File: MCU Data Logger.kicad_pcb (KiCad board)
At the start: 2 copper layers, 29 parts, among them J1 Conn_01x04_Pin, J2 Conn_01x04_Pin, J3 Conn_01x09_Pin, J4 Conn_02x03_Odd_Even, U1 24LC1025, U2 24LC1025, U3 ATmega328P, U4 DS1337S_, Y1 16MHz, Y2 32.768 KHz

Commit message: Components find there home
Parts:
- BT1: footprint TerminalBlock_Phoenix:TerminalBlock_Phoenix_MPT-0,5-2-2.54_1x02_P2.54mm_Horizontal -> Connector_PinHeader_2.54mm:PinHeader_2x01_P2.54mm_Vertical
- moved H1 118.7 mm to (167.5, 66.9)
- moved R7 99.6 mm to (160.5, 43.3)
- moved C4 95.8 mm to (160.5, 45.7)
- moved C3 94.6 mm to (154.3, 63.4)
- moved R3 93.9 mm to (154.3, 41.0)
- moved C2 91.4 mm to (149.7, 63.4)
- moved R2 90.7 mm to (150.7, 41.0), turned to 180 degrees
- moved C1 88.4 mm to (145.1, 63.4)
- moved R1 87.8 mm to (147.3, 41.0)
- moved R4 84.8 mm to (140.5, 63.4), turned to 180 degrees
- moved D1 82.6 mm to (160.5, 41.0)
- moved U3 81.4 mm to (150.9, 50.0)
- moved R5 79.4 mm to (135.9, 63.4), turned to 180 degrees
- moved J1 77.2 mm to (167.0, 52.6)
- moved J2 76.3 mm to (163.2, 67.6), turned to -90 degrees
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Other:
- board outline added: 43.2 x 33 mm

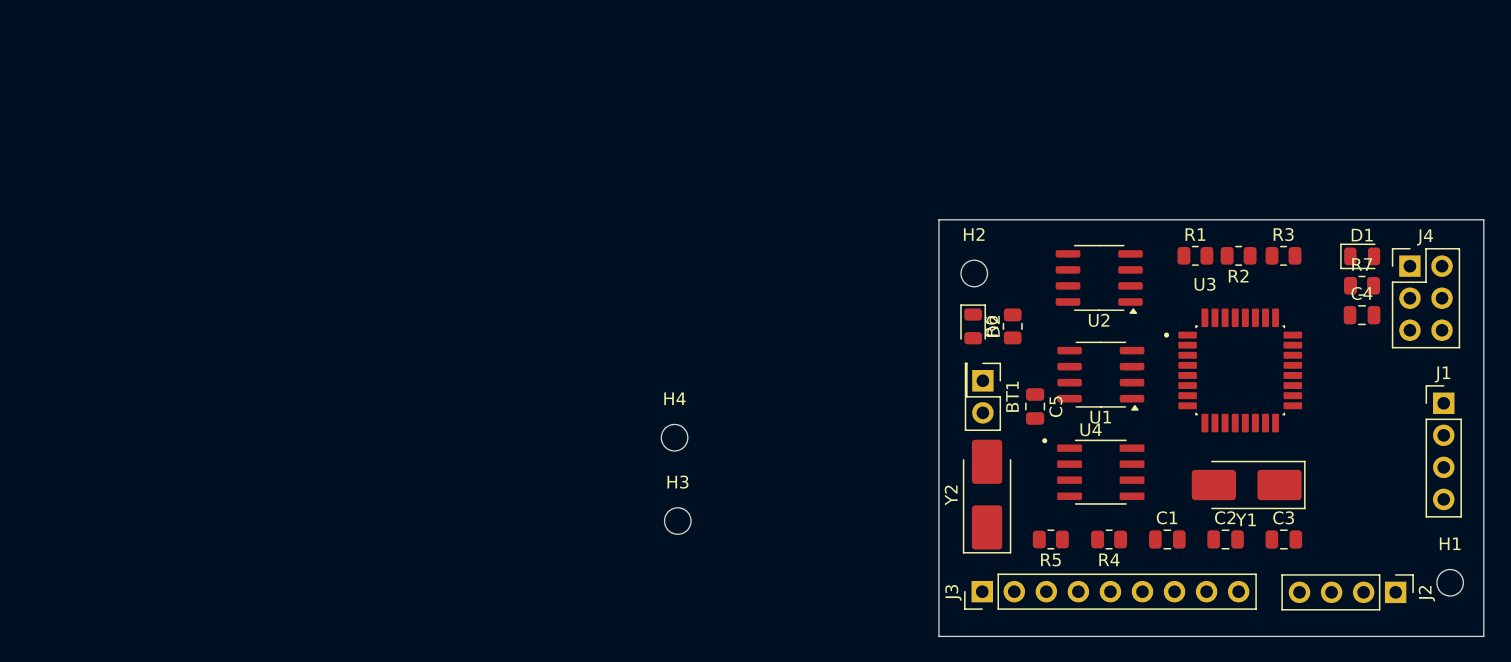
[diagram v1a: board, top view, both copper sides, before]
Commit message: adding outline
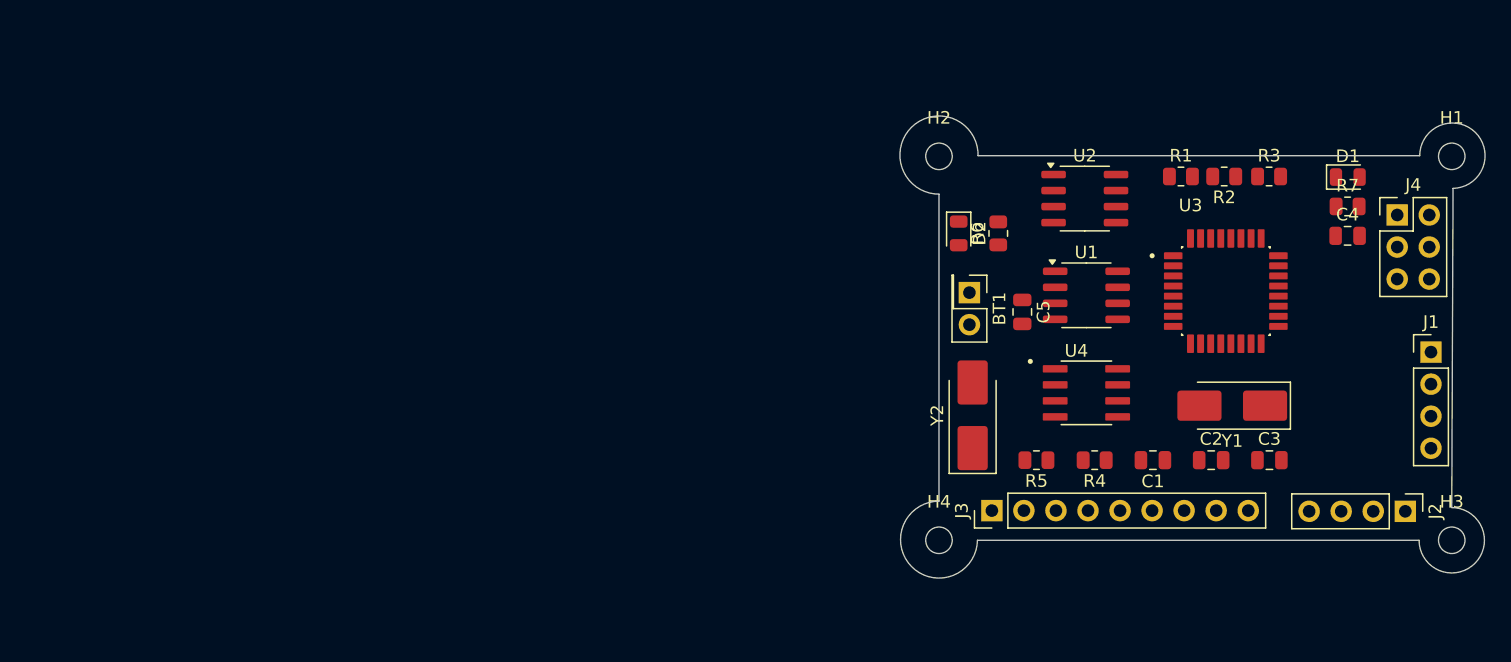
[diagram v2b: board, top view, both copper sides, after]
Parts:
- moved H3 61.4 mm to (167.6, 63.5)
- moved H1 33.8 mm to (167.6, 33.1)
- moved H4 22.5 mm to (127.0, 63.5)
- moved H2 9.70 mm to (127.0, 33.1)
- moved C5 7.56 mm to (133.6, 45.4)
- moved D2 7.46 mm to (128.6, 39.2)
- moved R6 7.46 mm to (131.7, 39.2)
- moved BT1 7.07 mm to (129.4, 43.9)
- moved J2 6.47 mm to (164.0, 61.2)
- moved J3 6.47 mm to (131.2, 61.1)
- moved C1 6.39 mm to (144.0, 57.1), turned to 180 degrees
- moved C3 6.39 mm to (153.2, 57.1)
- moved C4 6.39 mm to (159.4, 39.4)
- moved R1 6.39 mm to (146.2, 34.7)
- moved R2 6.39 mm to (149.6, 34.7)
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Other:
- board size 43.2 x 33 mm -> 46.4 x 36.6 mm
